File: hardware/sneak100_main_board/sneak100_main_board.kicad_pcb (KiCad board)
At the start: 2 copper layers, 68 x 75 mm, 81 parts, among them J1 Conn_01x06, J10 Conn_01x06, J11 Conn_01x03, J12 Conn_01x03, J13 Conn_01x03, J14 Conn_01x03, J2 Conn_01x06, J3 Conn_01x06, J4 Conn_01x06, J5 Conn_01x02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

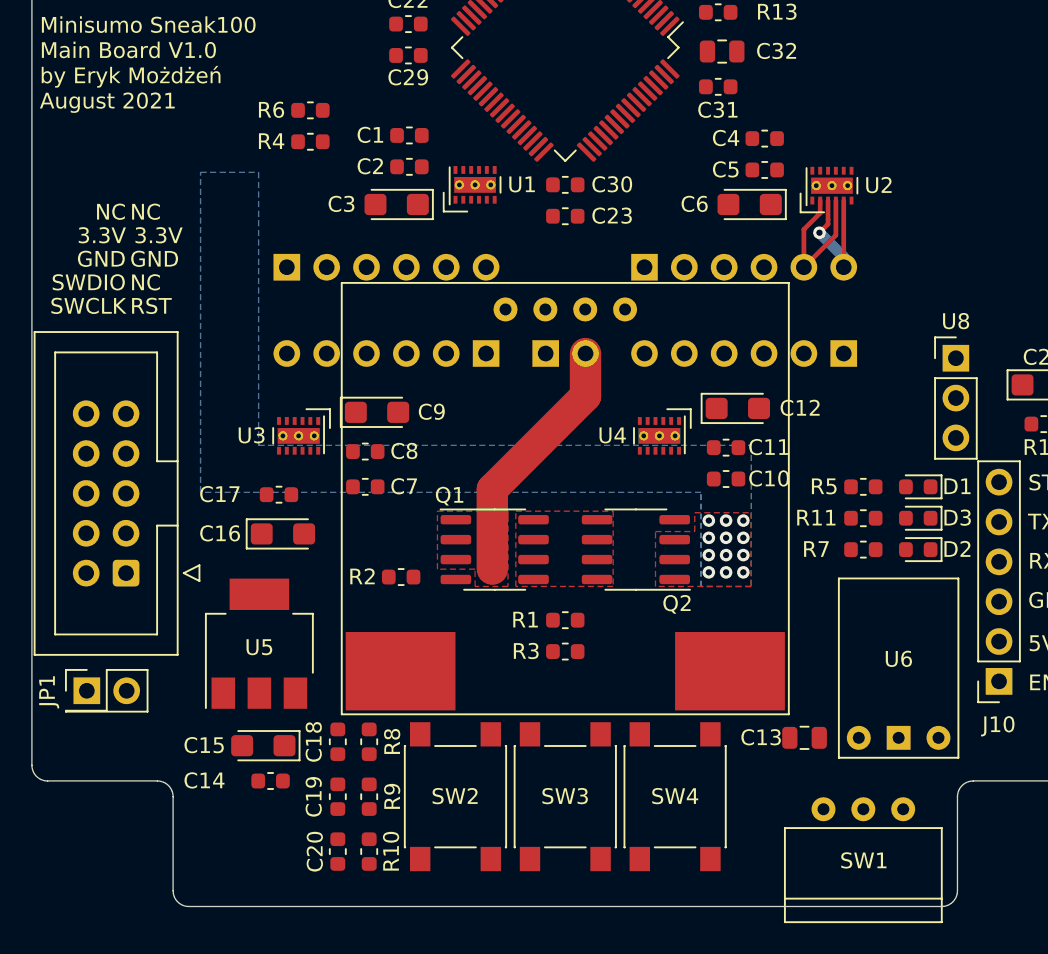
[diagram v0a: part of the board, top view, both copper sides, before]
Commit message: power rails routed
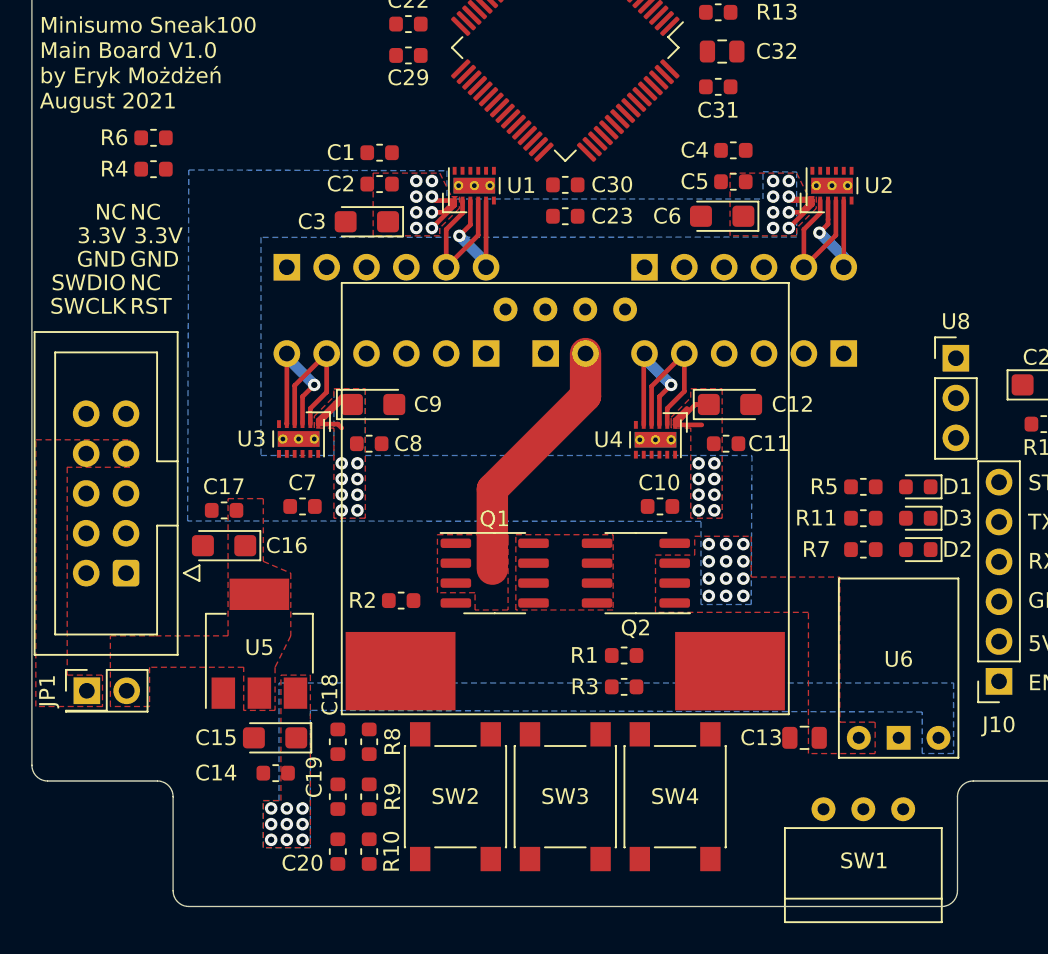
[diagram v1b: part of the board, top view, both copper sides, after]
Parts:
- moved R4 10.2 mm to (121.5, 69.5)
- moved R6 10.2 mm to (121.5, 67.5)
- moved C10 4.56 mm to (153.8, 91.0), turned to 180 degrees
- moved R1 4.37 mm to (151.5, 100.5)
- moved R3 4.37 mm to (151.5, 102.5)
- moved C7 4.19 mm to (131.0, 91.0), turned to 180 degrees
- moved C16 3.82 mm to (126.0, 93.5), turned to 180 degrees
- moved C17 3.64 mm to (126.0, 91.2), turned to 180 degrees
- moved C1 2.20 mm to (135.9, 68.5)
- moved C2 2.20 mm to (135.9, 70.5)
- moved C3 2.20 mm to (135.1, 72.8)
- moved C4 2.14 mm to (158.5, 68.3)
- moved C5 2.14 mm to (158.5, 70.3)
- moved C6 1.90 mm to (157.8, 72.5)
- moved Q1 1.50 mm to (143.2, 95.2)
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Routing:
- net SUPPLY: track 0.00 -> 25.8 mm, vias 12 -> 44
- net /motors/RB_OUT1: track 0.00 -> 10.4 mm
- net /motors/LB_OUT1: track 0.00 -> 10.3 mm
- net /motors/RB_OUT2: track 0.00 -> 10.1 mm, vias 0 -> 1
- net /motors/LB_OUT2: track 0.00 -> 10.1 mm, vias 0 -> 1
- net /motors/LF_OUT1: track 0.00 -> 9.78 mm
- net /motors/LF_OUT2: track 0.00 -> 9.49 mm, vias 0 -> 1
- net +5V: vias 0 -> 9
- added copper zone on F.Cu, net +3V3
- added copper zone on B.Cu, net +5V
- added copper zone on F.Cu, net +5V
- added copper zone on F.Cu, net ST-LINK_3.3V

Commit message: Motor signals and interface
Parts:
- moved R13 24.5 mm to (133.0, 59.2), turned to 0 degrees
- moved J11 20.5 mm to (119.8, 69.2)
- moved J14 19.4 mm to (171.5, 70.5)
- moved R4 13.3 mm to (129.0, 58.5)
- moved R6 13.3 mm to (129.0, 56.5)
- moved J12 11.2 mm to (117.5, 59.5), turned to 270 degrees
- moved J13 8.07 mm to (173.5, 59.5), turned to 270 degrees
- moved C24 8.00 mm to (161.8, 53.8)
- moved C25 8.00 mm to (161.8, 51.8)
- moved C26 8.00 mm to (168.8, 51.8)
- moved C27 8.00 mm to (165.2, 51.8)
- moved L1 8.00 mm to (158.0, 52.0)
- moved Y1 8.00 mm to (167.0, 55.0)
- moved C28 5.35 mm to (138.5, 51.2)
- moved C22 3.01 mm to (137.5, 57.2)
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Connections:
- U9 pad 14: /controller/RF_A -> /controller/RB_A
- U9 pad 15: /controller/RF_B -> /controller/RB_B
- U9 pad 29: /controller/RF_IN1 -> /controller/RB_IN1
- U9 pad 30: /controller/RF_IN2 -> /controller/RB_IN2
- U9 pad 58: /controller/RB_A -> /controller/RF_A
- U9 pad 59: /controller/RB_B -> /controller/RF_B
- U9 pad 61: /controller/RB_IN1 -> /controller/RF_IN1
- U9 pad 62: /controller/RB_IN2 -> /controller/RF_IN2
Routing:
- net /interface/BUTTON_R: track 0.00 -> 121.0 mm, vias 0 -> 2
- net /interface/BUTTON_C: track 0.00 -> 110.6 mm, vias 0 -> 2
- net /interface/BUTTON_L: track 0.00 -> 102.0 mm, vias 0 -> 2
- net /controller/RST: track 0.00 -> 80.8 mm, vias 0 -> 2
- net /controller/SWCLK: track 0.00 -> 70.8 mm, vias 0 -> 1
- net /controller/SWDIO: track 0.00 -> 64.2 mm, vias 0 -> 1
- net /interface/LED_RUN: track 0.00 -> 48.7 mm, vias 0 -> 2
- net /interface/LED_ERROR: track 0.00 -> 46.7 mm, vias 0 -> 2
- net /controller/LF_A: track 0.00 -> 24.0 mm, vias 0 -> 2
- net /controller/LF_B: track 0.00 -> 23.1 mm, vias 0 -> 2
- net /controller/RF_IN2: track 0.00 -> 20.8 mm, vias 0 -> 3
- net /controller/I2C3_SDA: track 0.00 -> 20.5 mm, vias 0 -> 2
- net /controller/RF_IN1: track 0.00 -> 19.3 mm, vias 0 -> 3
- net +3V3: track 0.00 -> 18.3 mm
- net /controller/I2C3_SCL: track 0.00 -> 16.9 mm
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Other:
- board text added: "JLCJLCJLCJLC"

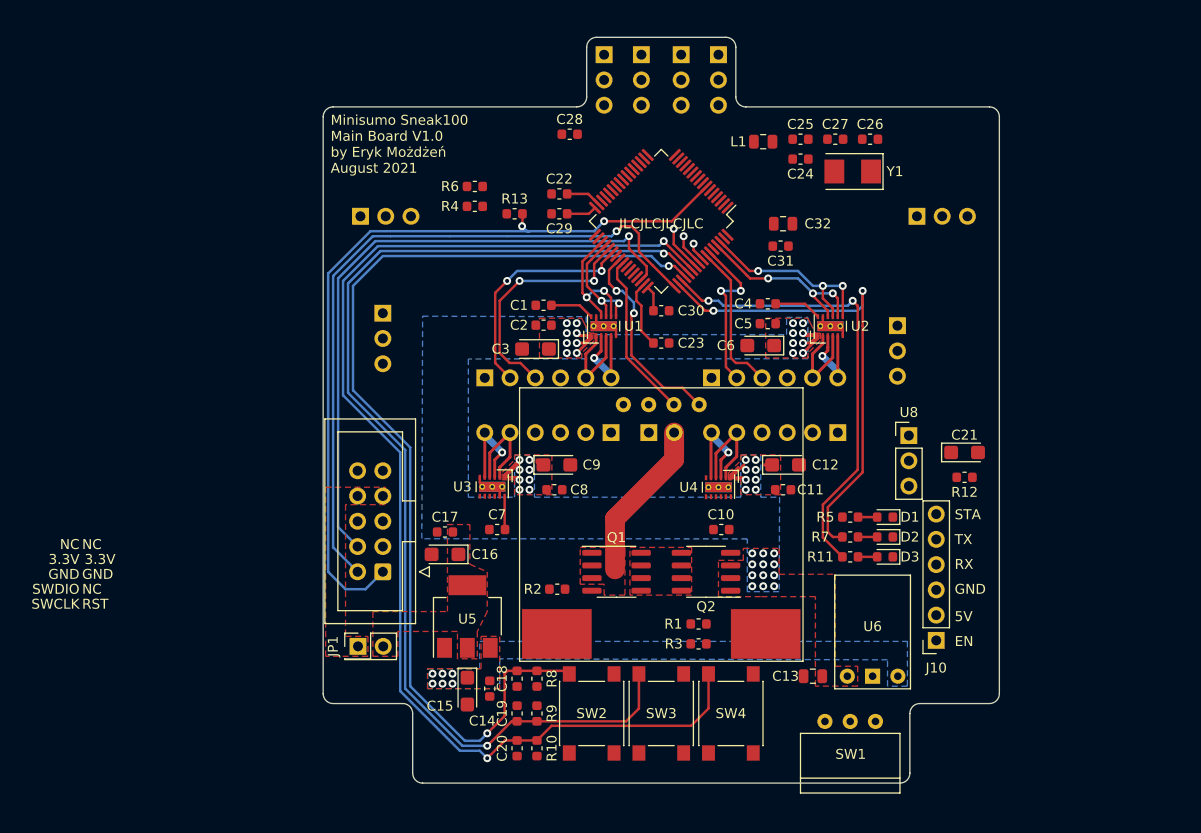
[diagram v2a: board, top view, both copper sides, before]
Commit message: Remaining signals from uC
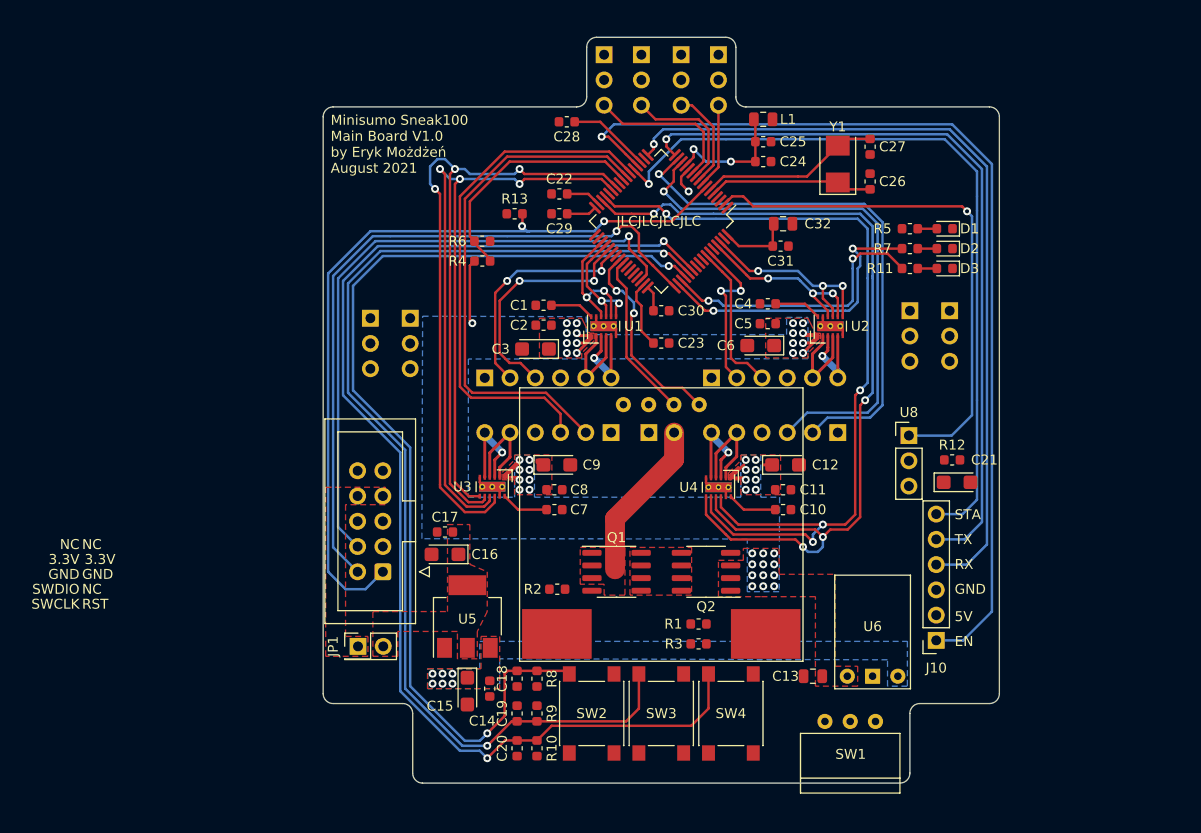
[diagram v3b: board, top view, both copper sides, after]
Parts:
- moved D1 29.6 mm to (176.2, 60.8)
- moved D2 29.6 mm to (176.2, 62.8)
- moved D3 29.6 mm to (176.2, 64.8)
- moved R11 29.6 mm to (172.8, 64.8)
- moved R5 29.6 mm to (172.8, 60.8)
- moved R7 29.6 mm to (172.8, 62.8)
- moved J12 11.4 mm to (122.5, 69.8), turned to 180 degrees
- moved J13 9.53 mm to (172.8, 69.0), turned to 180 degrees
- moved C10 6.53 mm to (160.0, 89.0), turned to 0 degrees
- moved C7 6.09 mm to (137.0, 89.0), turned to 0 degrees
- moved R4 5.55 mm to (129.8, 64.0)
- moved R6 5.55 mm to (129.8, 62.0), turned to 0 degrees
- moved J14 5.46 mm to (176.8, 69.0)
- moved C26 4.25 mm to (168.8, 56.0), turned to 90 degrees
- moved C24 3.76 mm to (158.0, 54.0)
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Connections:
- U9 pad 10: /controller/LINE_RM -> /controller/LINE_LM
- U9 pad 11: /controller/LINE_RR -> /controller/LINE_LL
- U9 pad 25: /controller/PROXIMITY_RR -> /controller/PROXIMITY_FL
- U9 pad 56: /controller/PROXIMITY_FL -> /controller/PROXIMITY_RR
- U9 pad 8: /controller/LINE_LL -> /controller/LINE_RR
- U9 pad 9: /controller/LINE_LM -> /controller/LINE_RM
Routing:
- net /controller/BLUETOOTH_EN: track 0.00 -> 98.0 mm, vias 0 -> 1
- net /controller/LB_IN1: track 0.00 -> 97.4 mm, vias 0 -> 3
- net /controller/RB_IN2: track 0.00 -> 92.9 mm, vias 0 -> 4
- net /controller/LB_IN2: track 0.00 -> 90.5 mm, vias 0 -> 3
- net /controller/RB_IN1: track 0.00 -> 87.9 mm, vias 0 -> 4
- net /interface/BLUETOOTH_TX: track 0.00 -> 81.3 mm, vias 0 -> 1
- net /controller/BLUETOOTH_STATUS: track 0.00 -> 76.8 mm, vias 0 -> 1
- net /interface/BLUETOOTH_RX: track 0.00 -> 76.2 mm, vias 0 -> 1
- net /controller/RB_A: track 0.00 -> 54.9 mm, vias 0 -> 1
- net /controller/RB_B: track 0.00 -> 53.7 mm, vias 0 -> 1
- net /controller/RECEIVER_OUT: track 0.00 -> 53.3 mm, vias 0 -> 1
- net /controller/LB_A: track 0.00 -> 52.1 mm
- net /controller/LB_B: track 0.00 -> 51.7 mm
- net /controller/BATTERY_SENSE: track 0.00 -> 24.7 mm
- net +3V3: track 18.3 -> 40.3 mm
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
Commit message: proximity sensors connectors
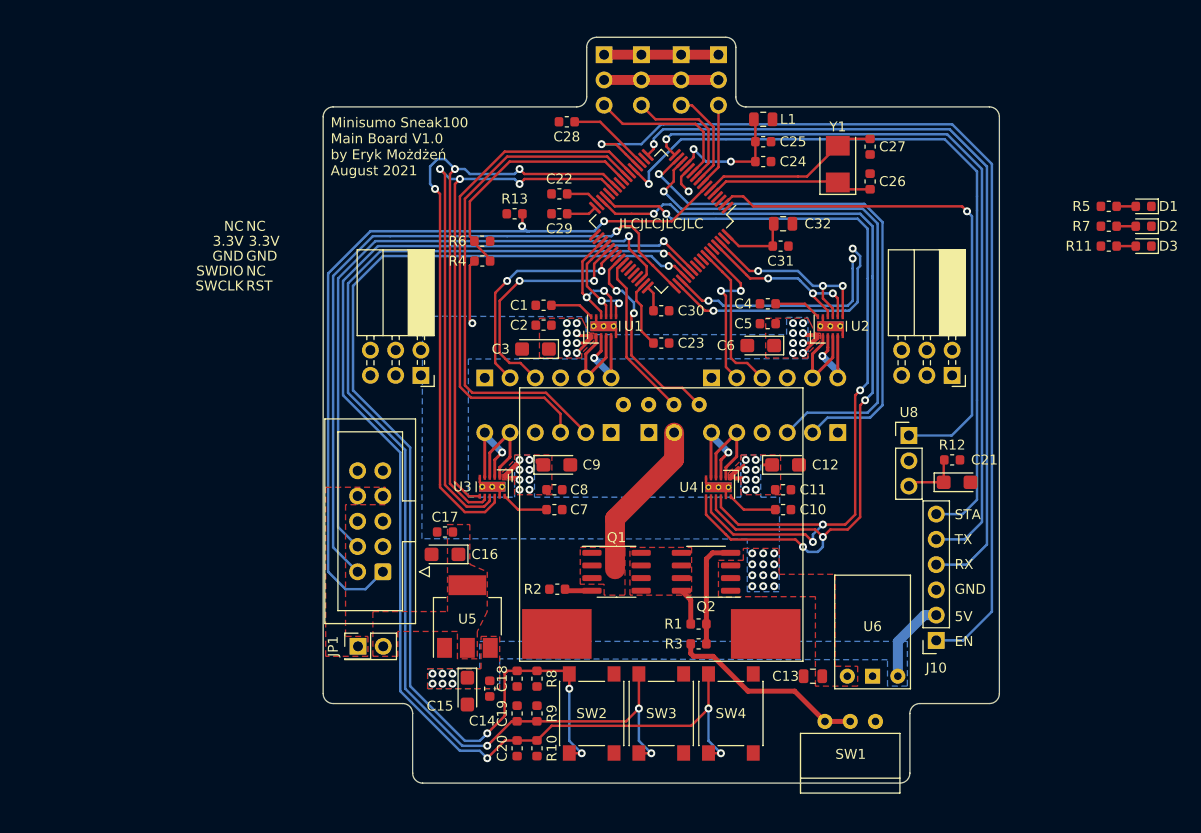
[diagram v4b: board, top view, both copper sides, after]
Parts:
- removed J13, J14: Conn_01x03, Connector_PinHeader_2.54mm:PinHeader_1x03_P2.54mm_Vertical
- J11, J12: value Conn_01x03 -> Conn_02x03_Odd_Even; footprint Connector_PinHeader_2.54mm:PinHeader_1x03_P2.54mm_Vertical -> Connector_PinSocket_2.54mm:PinSocket_2x03_P2.54mm_Horizontal; moved to F.Cu
- J6, J7, J8, J9: footprint Connector_PinHeader_2.54mm:PinHeader_1x03_P2.54mm_Vertical -> Connector_PinSocket_2.54mm:PinSocket_1x03_P2.54mm_Vertical
- moved J12 54.8 mm to (177.0, 75.5), turned to 270 degrees
- moved D1 20.1 mm to (196.2, 58.5)
- moved D2 20.1 mm to (196.2, 60.5)
- moved D3 20.1 mm to (196.2, 62.5)
- moved R11 20.1 mm to (192.8, 62.5)
- moved R5 20.1 mm to (192.8, 58.5)
- moved R7 20.1 mm to (192.8, 60.5)
- moved J11 7.67 mm to (123.6, 75.5), turned to 270 degrees
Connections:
- J11 pad 2: +3V3 -> GND
- J11 pad 3: /controller/PROXIMITY_LL -> +3V3
- J12 pad 2: +3V3 -> GND
- J12 pad 3: /controller/PROXIMITY_FL -> +3V3
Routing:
- net Net-(R3-Pad2): track 0.00 -> 19.8 mm
- net GND: track 14.6 -> 26.1 mm
- net +3V3: track 40.3 -> 51.8 mm
- net Net-(Q2-Pad4): track 0.00 -> 11.2 mm
- net /interface/BUTTON_L: track 102.0 -> 111.7 mm, vias 2 -> 4
- net +5V: track 0.00 -> 8.44 mm
- net /interface/BUTTON_R: track 121.0 -> 127.2 mm, vias 2 -> 4
- net /interface/BUTTON_C: track 110.6 -> 116.9 mm, vias 2 -> 4
- net Net-(C21-Pad1): track 0.00 -> 5.93 mm
- net /interface/LED_ERROR: track 28.5 -> 23.0 mm
- net /interface/LED_RUN: track 30.3 -> 25.3 mm
- net Net-(Q1-Pad5): track 0.00 -> 3.73 mm
- net Net-(Q1-Pad4): track 0.00 -> 2.76 mm

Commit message: programmer connector, proximity sensors routed
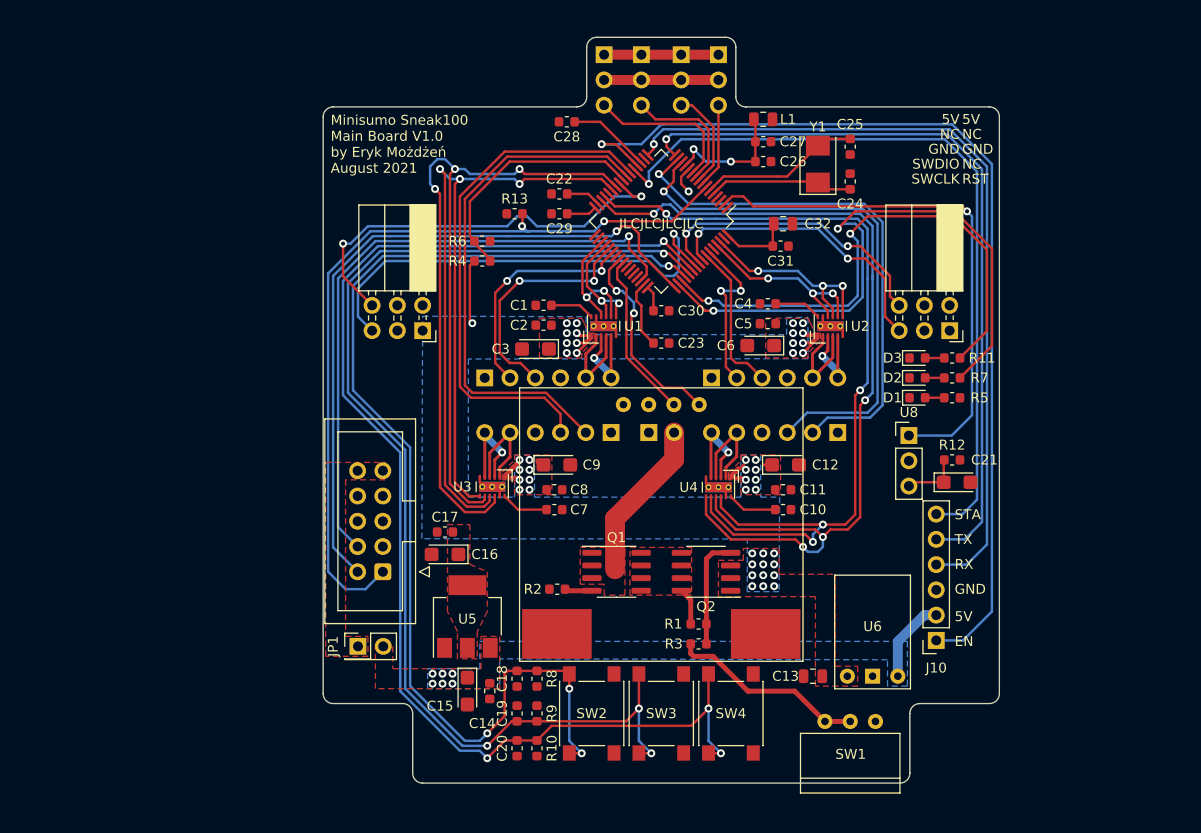
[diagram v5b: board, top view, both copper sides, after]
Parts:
- removed MCU1: Conn_02x05_Counter_Clockwise, Connector_IDC:IDC-Header_2x05_P2.54mm_Vertical
- added J13: Conn_02x05_Odd_Even, Connector_IDC:IDC-Header_2x05_P2.54mm_Vertical, F.Cu at (119.8, 95.2)
- moved D1 29.8 mm to (173.5, 77.8), turned to 0 degrees
- moved D2 27.4 mm to (173.5, 75.8), turned to 0 degrees
- moved D3 25.4 mm to (173.5, 73.8), turned to 0 degrees
- moved R5 24.9 mm to (177.0, 77.8), turned to 180 degrees
- moved R7 21.9 mm to (177.0, 75.8), turned to 0 degrees
- moved R11 19.4 mm to (177.0, 73.8), turned to 0 degrees
- moved J12 4.51 mm to (176.8, 71.0)
- moved J11 4.50 mm to (123.8, 71.0)
- moved C24 2.00 mm to (166.8, 56.0)
- moved C25 2.00 mm to (166.8, 52.5)
- moved Y1 2.00 mm to (163.5, 54.2)
- moved C14 0.25 mm to (130.5, 107.2)
- renumbered C26 to C24, C27 to C25, C24 to C26, C25 to C27
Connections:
- JP1 pad 1: ST-LINK_3.3V -> ST-LINK_5V
- JP1 pad 2: +3V3 -> +5V
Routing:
- net /controller/PROXIMITY_LL: track 0.00 -> 47.2 mm, vias 0 -> 1
- net /controller/PROXIMITY_FL: track 0.00 -> 43.0 mm, vias 0 -> 2
- net /interface/LED_RUN: track 25.3 -> 62.0 mm
- net /interface/LED_ERROR: track 23.0 -> 53.6 mm
- net /controller/PROXIMITY_RR: track 0.00 -> 29.9 mm, vias 0 -> 2
- net /controller/PROXIMITY_FR: track 0.00 -> 29.8 mm, vias 0 -> 2
- net Net-(C25-Pad1): track 18.2 -> 16.2 mm
- net Net-(C24-Pad1): track 16.6 -> 14.6 mm
- added copper zone on F.Cu, net ST-LINK_5V
- removed copper zone on F.Cu, net ST-LINK_3.3V
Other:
- board text removed: "3.3V"
